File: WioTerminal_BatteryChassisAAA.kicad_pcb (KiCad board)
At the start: 2 copper layers, 67.5 x 52.6 mm, 0 parts

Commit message: Revision A
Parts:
- added C1: 10u, Capacitor_SMD:C_0805_2012Metric, F.Cu at (10.6, -13.9)
- added C10: 100n, Capacitor_SMD:C_0603_1608Metric, F.Cu at (20.8, -19.9)
- added C12: 1u, Capacitor_SMD:C_0603_1608Metric, B.Cu at (29.0, -39.2)
- added C13: 1u, Capacitor_SMD:C_0603_1608Metric, B.Cu at (14.9, -39.2)
- added C2: 100n, Capacitor_SMD:C_0603_1608Metric, F.Cu at (17.6, -12.8)
- added C3: 10u, Capacitor_SMD:C_0805_2012Metric, F.Cu at (10.6, -15.9)
- added C4: 10u, Capacitor_SMD:C_0805_2012Metric, F.Cu at (20.8, -22.2)
- added C5: 100n, Capacitor_SMD:C_0603_1608Metric, F.Cu at (15.8, -22.4)
- added C6: 10p, Capacitor_SMD:C_0603_1608Metric, F.Cu at (16.7, -26.6)
- added C7: 22u, Capacitor_SMD:C_1206_3216Metric, F.Cu at (10.6, -24.4)
- added C8: 22u, Capacitor_SMD:C_1206_3216Metric, F.Cu at (10.6, -26.8)
- added C9: 22u, Capacitor_SMD:C_1206_3216Metric, F.Cu at (10.6, -29.1)
- added F1: 1A, Fuse:Fuse_1812_4532Metric, F.Cu at (9.74, -7.25)
- added J1: Raspberry_Pi_2_3, Connector_PinHeader_2.54mm:PinHeader_2x20_P2.54mm_Vertical_SMD, F.Cu at (34.0, -41.5)
- added J2: Ext. BAT, local:PinHeader_1x02_P2.54mm_Horizontal, B.Cu at (3.46, -11.4)
- added J3: GROVE, local:PHS-4AW, B.Cu at (31.0, -44.2)
- added J4: GROVE, local:PHS-4AW, B.Cu at (17.0, -44.2)
- added L1: 1u, 2.5A, local:74438323010, F.Cu at (7.40, -19.9)
- added LOGO1: Logo_Open_Hardware_Small, local:logo, B.Cu at (31.8, -5.25)
- added MH1: Corner, local:MountingHole_2.2mm_M2_DIN965_Mask, F.Cu at (3.50, -3.50)
- added MH2: Corner, local:MountingHole_2.2mm_M2_DIN965_Mask, F.Cu at (64.5, -3.50)
- added MH3: Corner, local:MountingHole_2.2mm_M2_DIN965_Mask, F.Cu at (64.5, -49.0)
- added MH4: Corner, local:MountingHole_2.2mm_M2_DIN965_Mask, F.Cu at (3.50, -49.0)
- added R1: 0.04, Resistor_SMD:R_0805_2012Metric, F.Cu at (14.6, -10.5)
- added R10: 1M, Resistor_SMD:R_0603_1608Metric, F.Cu at (16.2, -16.9)
- added R11: 0, Resistor_SMD:R_0603_1608Metric, F.Cu at (42.0, -34.9)
- added R12: 0, Resistor_SMD:R_0603_1608Metric, F.Cu at (42.0, -48.2)
- added R13: DNP, Resistor_SMD:R_0603_1608Metric, F.Cu at (18.4, -33.0)
- added R14: DNP, Resistor_SMD:R_0603_1608Metric, F.Cu at (18.4, -34.9)
- added R15: 100k, Resistor_SMD:R_0805_2012Metric, F.Cu at (15.1, -14.2)
- added R2: 4.7k, Resistor_SMD:R_0603_1608Metric, F.Cu at (29.2, -33.0)
- added R3: 0, Resistor_SMD:R_0603_1608Metric, F.Cu at (26.8, -10.0)
- added R4: DNP, Resistor_SMD:R_0603_1608Metric, F.Cu at (26.8, -6.64)
- added R5: 4.7k, Resistor_SMD:R_0603_1608Metric, F.Cu at (29.2, -34.9)
- added R6: 0, Resistor_SMD:R_0603_1608Metric, F.Cu at (24.6, -10.0)
- added R7: DNP, Resistor_SMD:R_0603_1608Metric, F.Cu at (24.6, -6.64)
- added R8: 1M, Resistor_SMD:R_0603_1608Metric, F.Cu at (14.2, -27.4)
- added R9: 111k, Resistor_SMD:R_0603_1608Metric, F.Cu at (15.0, -24.8)
- added SW1: JS102011JAQN, local:JS102011JAQN, B.Cu at (4.00, -38.2)
- added TP1: BAT, TestPoint:TestPoint_Pad_D1.0mm, F.Cu at (12.1, -11.4)
- added TP2: BAT-GND, TestPoint:TestPoint_Pad_D1.0mm, F.Cu at (9.60, -11.4)
- added TP3: +5V, TestPoint:TestPoint_Pad_D1.0mm, F.Cu at (14.3, -29.9)
- added TP4: +5V-GND, TestPoint:TestPoint_Pad_D1.0mm, F.Cu at (6.50, -29.1)
- added U1: INA219, Package_TO_SOT_SMD:SOT-23-8, F.Cu at (20.4, -11.2)
- added U2: TPS63060, Package_SON:Texas_S-PWSON-N10_ThermalVias, F.Cu at (12.4, -19.9)
- added U3: ATECC608A, Package_DFN_QFN:DFN-8-1EP_3x2mm_P0.5mm_EP1.3x1.5mm, F.Cu at (20.8, -16.4)
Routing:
- net +3V3: track 0.00 -> 72.5 mm, vias 0 -> 4
- net /SCL: track 0.00 -> 60.6 mm
- net /SDA: track 0.00 -> 53.0 mm, vias 0 -> 4
- net Net-(R15-Pad2): track 0.00 -> 47.3 mm, vias 0 -> 3
- net Net-(C1-Pad1): track 0.00 -> 47.0 mm, vias 0 -> 1
- net +5V: track 0.00 -> 44.8 mm
- net /I2C1_SDA: track 0.00 -> 23.5 mm, vias 0 -> 1
- net /TXD: track 0.00 -> 21.8 mm, vias 0 -> 1
- net GND: track 0.00 -> 17.0 mm, vias 0 -> 142
- net /RXD: track 0.00 -> 16.7 mm, vias 0 -> 1
- net /I2C1_SCL: track 0.00 -> 14.4 mm, vias 0 -> 1
- net /A0: track 0.00 -> 7.79 mm
- net Net-(C6-Pad1): track 0.00 -> 7.34 mm
- net /A1: track 0.00 -> 5.32 mm
- net Net-(F1-Pad1): track 0.00 -> 4.96 mm
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- added copper zone on F.Cu, net +5V
- added copper zone on B.Cu, net GND
- added copper zone on F.Cu, net GND
- added copper zone on F.Cu, net Net-(C1-Pad1)
- added copper zone on F.Cu, net Net-(F1-Pad1)
- added copper zone on F.Cu, net Net-(F1-Pad2)
- added copper zone on F.Cu, net Net-(L1-Pad1)
- added copper zone on F.Cu, net Net-(L1-Pad2)
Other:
- board size 67.5 x 52.6 mm -> 68 x 52.5 mm
- board text added: "+5V"
- board text added: "3.3V"
- board text added: "AA/AAA Battery Chassis for Wio Terminal 2020-05-28 Rev.A by Kenta IDA (@ciniml)"
- board text added: "ON"
- board text added: "RxD"
- board text added: "SCL"
- board text added: "SDA"
- board text added: "TxD"

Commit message: Fix wrong INA-219 pin assignment
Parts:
- TP1, TP2, TP3, TP4: footprint TestPoint:TestPoint_Pad_D1.0mm -> TestPoint:TestPoint_THTPad_D1.0mm_Drill0.5mm
- moved J2 3.10 mm to (3.60, -8.35)
- moved F1 2.75 mm to (12.3, -6.25)
- turned U1 to 0 degrees
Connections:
- SW1 pad 1: Net-(SW1-Pad1) -> Net-(R15-Pad2)
- SW1 pad 3: Net-(R15-Pad2) -> Net-(SW1-Pad3)
- U1 pad 1: /A1 -> Net-(F1-Pad1)
- U1 pad 2: /A0 -> Net-(C1-Pad1)
- U1 pad 3: /SDA -> GND
- U1 pad 4: /SCL -> +3V3
- U1 pad 5: +3V3 -> /SCL
- U1 pad 6: GND -> /SDA
- U1 pad 7: Net-(C1-Pad1) -> /A0
- U1 pad 8: Net-(F1-Pad1) -> /A1
- U3 pad 5: /SCL -> /SDA
- U3 pad 6: /SDA -> /SCL
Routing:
- net Net-(C1-Pad1): track 47.0 -> 63.0 mm
- net +3V3: track 72.5 -> 62.8 mm, vias 4 -> 2
- net /A0: track 7.79 -> 1.83 mm
- net Net-(R15-Pad2): track 47.3 -> 42.3 mm
- net /A1: track 5.32 -> 1.83 mm
- net /SCL: track 60.6 -> 61.2 mm
- net /SDA: track 53.0 -> 52.4 mm
- net GND: vias 142 -> 136

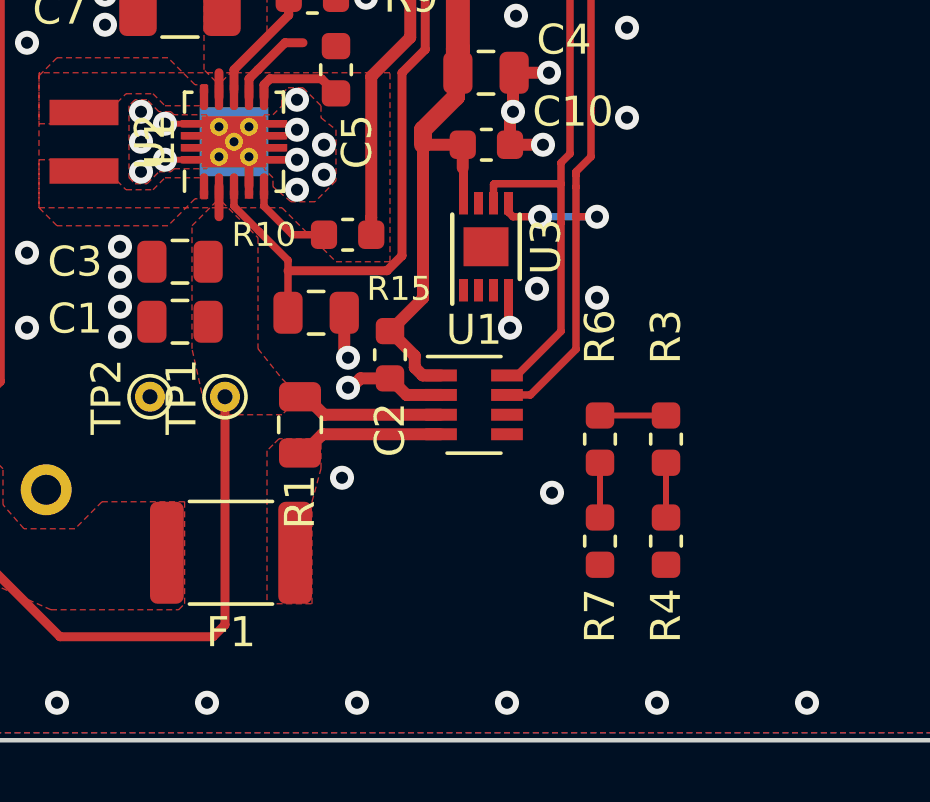
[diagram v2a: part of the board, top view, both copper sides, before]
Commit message: Fix INA-219 connection
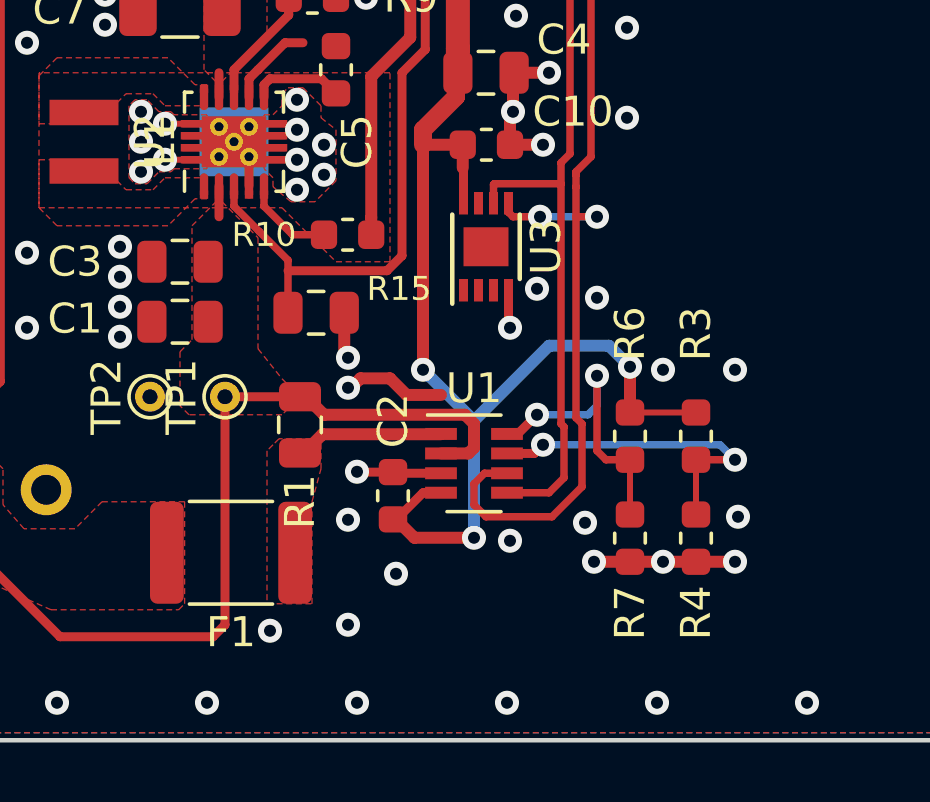
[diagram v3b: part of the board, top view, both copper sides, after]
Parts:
- moved C2 4.70 mm to (17.7, -8.15), turned to 90 degrees
- moved U1 1.95 mm to (20.4, -9.23)
- moved R3 1.00 mm to (27.8, -10.1)
- moved R4 1.00 mm to (27.8, -6.74)
- moved R6 1.00 mm to (25.6, -10.1)
- moved R7 1.00 mm to (25.6, -6.74)
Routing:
- net +3V3: track 62.8 -> 80.3 mm, vias 2 -> 5
- net /A0: track 1.83 -> 11.1 mm, vias 0 -> 2
- net /A1: track 1.83 -> 9.94 mm, vias 0 -> 2
- net /SDA: track 52.4 -> 60.3 mm
- net GND: track 17.0 -> 24.6 mm, vias 136 -> 147
- net Net-(C1-Pad1): track 63.0 -> 68.7 mm
- net /SCL: track 61.2 -> 65.8 mm
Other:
- board text added: "AA/AAA Battery Chassis for Wio Terminal 2020-07-16 Rev.B by Kenta IDA (@ciniml)"
- board text removed: "AA/AAA Battery Chassis for Wio Terminal 2020-05-28 Rev.A by Kenta IDA (@ciniml)"
